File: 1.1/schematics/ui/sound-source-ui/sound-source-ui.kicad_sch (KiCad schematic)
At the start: 14 parts

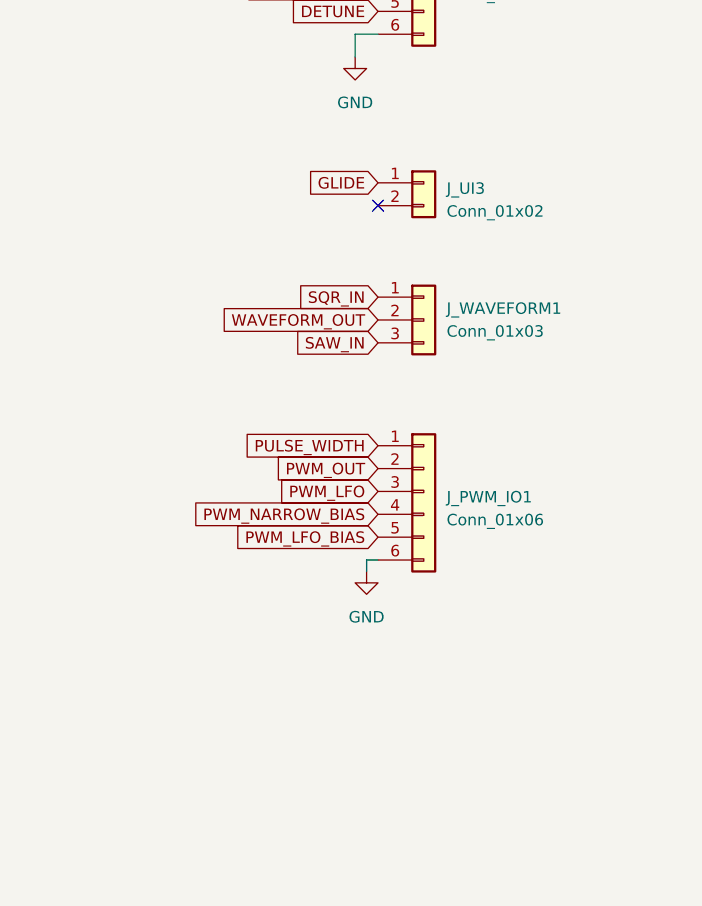
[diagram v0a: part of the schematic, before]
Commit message: Added envelope UI connections
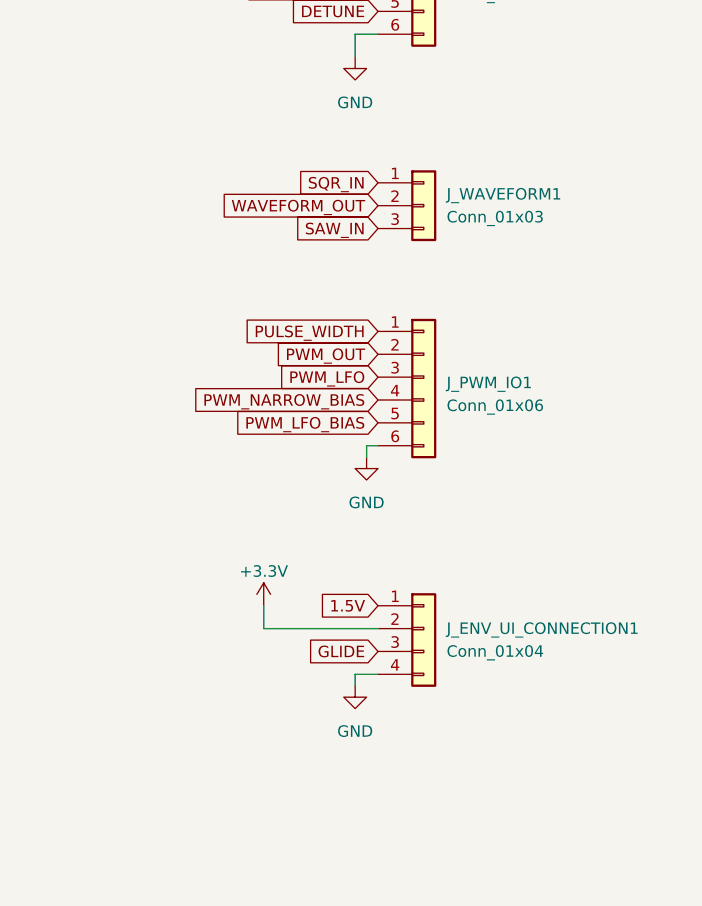
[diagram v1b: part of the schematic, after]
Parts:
- removed J_UI3: Conn_01x02, Shmoergh_Custom_Footprints:NSL25_01x02_Vertical, symbol Connector_Generic:Conn_01x02
- added J_ENV_UI_CONNECTION1: Conn_01x04, Shmoergh_Custom_Footprints:NSL25_01x04_Vertical, symbol Connector_Generic:Conn_01x04
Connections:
- net +3.3V: now also J_ENV_UI_CONNECTION1.2 (Pin_2)
- net 1.5V: now also J_ENV_UI_CONNECTION1.1 (Pin_1)
- net GLIDE: now also J_ENV_UI_CONNECTION1.3 (Pin_3)
- net GND: now also J_ENV_UI_CONNECTION1.4 (Pin_4)
- no-connect marks 20 -> 19
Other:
- moved on the sheet: J_PWM_IO1, J_WAVEFORM1
